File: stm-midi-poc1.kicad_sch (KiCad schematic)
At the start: 0 parts

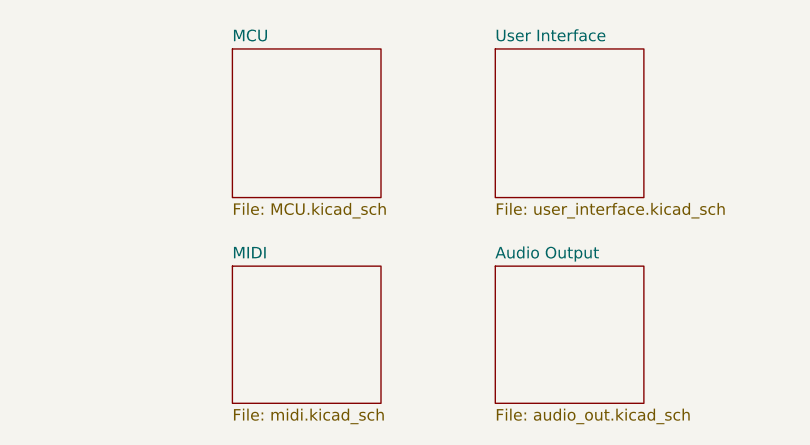
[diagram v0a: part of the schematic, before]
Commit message: Create PCB outline and move components into better locations. (Not done yet!) Update schematic a little bit with additional nets and clarifications. Add mounting holes. Unify components/footprints.
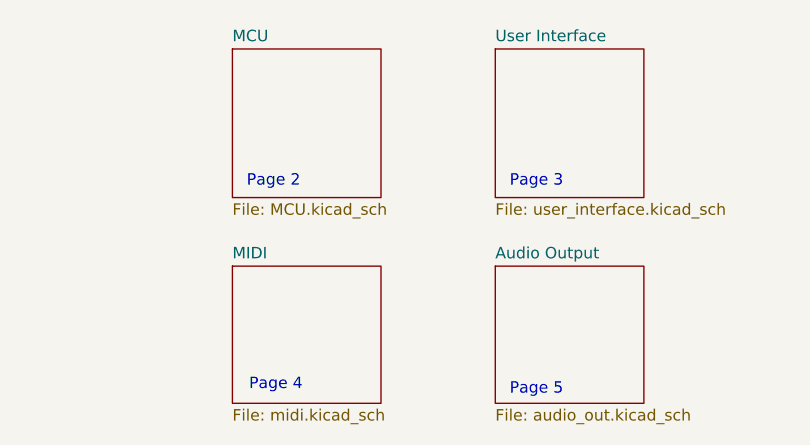
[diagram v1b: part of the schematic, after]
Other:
- note added: "Page 2"
- note added: "Page 3"
- note added: "Page 4"
- note added: "Page 5"
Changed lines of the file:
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@@
 	(title_block
 		(title "Block Diagram")
-		(date "2024-09-28")
+		(date "2024-10-12")
 		(rev "1")
 		(company "Douglas P. Fields, Jr.")
@@
 		)
 	)
+	(text "Page 5"
+		(exclude_from_sim no)
+		(at 239.522 162.306 0)
+		(effects
+			(font
+				(size 1.27 1.27)
+			)
+		)
+	)
+	(text "Page 3\n"
+		(exclude_from_sim no)
+		(at 239.522 139.192 0)
+		(effects
+			(font
+				(size 1.27 1.27)
+			)
+		)
+	)
+	(text "Page 2"
+		(exclude_from_sim no)
+		(at 210.312 139.192 0)
+		(effects
+			(font
+				(size 1.27 1.27)
+			)
+		)
+	)
+	(text "Page 4"
+		(exclude_from_sim no)
+		(at 210.566 161.798 0)
+		(effects
+			(font
+				(size 1.27 1.27)
+			)
+		)
+	)

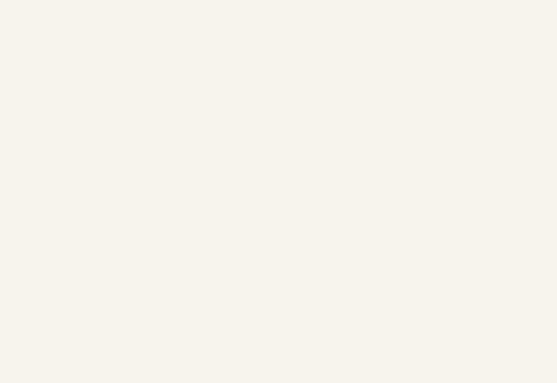
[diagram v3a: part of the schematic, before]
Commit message: Received EVT #1 boards. Updating based on errors found so far. Added revision page. First error was misunderstanding the TRS connector pinout/schematic.
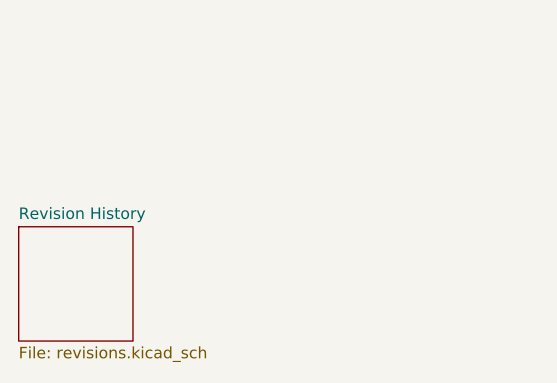
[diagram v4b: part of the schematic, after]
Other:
- added sheet Revision History (revisions.kicad_sch)
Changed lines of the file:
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@@
 	(title_block
 		(title "Block Diagram")
-		(date "2024-11-02")
-		(rev "1")
+		(date "2024-11-05")
+		(rev "2")
 		(company "Douglas P. Fields, Jr.")
 		(comment 1 "symbolics@lisp.engineer")
@@
 			)
 		)
+	)
+	(sheet
+		(at 25.4 177.8)
+		(size 12.7 12.7)
+		(fields_autoplaced yes)
+		(stroke
+			(width 0.1524)
+			(type solid)
+		)
+		(fill
+			(color 0 0 0 0.0000)
+		)
+		(property "Sheetname" "Revision History"
+			(at 25.4 177.0884 0)
+			(effects
+				(font
+					(size 1.27 1.27)
+				)
+				(justify left bottom)
+			)
+		)
+		(property "Sheetfile" "revisions.kicad_sch"
+			(at 25.4 191.0846 0)
+			(effects
+				(font
+					(size 1.27 1.27)
+				)
+				(justify left top)
+			)
+		)
+		(instances
+			(project "stm-midi-poc1"
+				(path "/7cd74113-1f92-4dcc-8610-19aa9fc81e5f"
+					(page "6")
+				)
+			)
+		)
